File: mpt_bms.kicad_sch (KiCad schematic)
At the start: 25 parts, among them U4 TPS62590, U5 BQ25185, U6 BQ27441-G1

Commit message: Added Display
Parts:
- C2: renamed from C109; footprint passive:C_0603 -> passive:C_0805; symbol db:capacitor/01.018.0025.0003 -> db:capacitor/01.018.0008.0004; Dist1# 311-1785-1-ND -> 311-1885-1-ND; FP C_0603 -> C_0805; MFR# CC0603KRX5R7BB475 -> CC0805KKX7R8BB475; Modified 2026-03-22 17:14:39 -> 2026-10-07 15:04:34; Rating 16V 10% -> 25V 10%; Series CC-X7R -> CC-X5R
- C8: renamed from C3; symbol db:capacitor/01.018.0025.0002 -> db:capacitor/01.018.0025.0013; Dist1# 311-1446-1-ND -> 311-2082-1-ND; MFR# CC0603KRX7R7BB105 -> CC0603KRX7R9BB105; Modified 2026-03-22 17:11:33 -> 2026-10-07 18:52:36; Rating 16V 10% -> 50V 10%
- D1: value Orange -> Red; footprint diode:D_0603 -> diode:LED_0805_Right_Angle; symbol db:diode/05.035.0031.0003 -> db:diode/05.035.0031.0004; Dist1# 160-1434-1-ND -> 160-1469-1-ND; Dist2 mouser -> none; FP D_0603 -> LED_0805_Right_Angle; MFR# LTST-C190KFKT -> LTST-S220KRKT; Modified 2026-03-23 15:41:47 -> 2026-10-06 21:05:36; Rating 2v 20mA 605nm -> 20mA; Version 2 -> 1
- R10: renamed from R15; symbol db:resistor/00.018.0009.0034 -> db:resistor_0603/00.018.0009.0578; Dist1# 13-RT0603FRE07619KLCT-ND -> 311-619KHRCT-ND; MFR# RT0603FRE07619KL -> RC0603FR-07619KL; Modified 2026-09-18 19:20:11 -> 2026-10-07 14:47:41; Rating 100mW, 1% -> 125mW, 1%; Remarks (none) -> Autogenerated; Version 1 -> 2
- R11: renamed from R16; symbol db:resistor/00.018.0009.0025 -> db:resistor_0603/00.018.0009.0139; Modified 2026-07-27 12:47:10 -> 2026-10-07 14:47:41; Rating 100mW, 1% -> 125mW, 1%; Remarks (none) -> Autogenerated
- R12: renamed from R17; symbol db:resistor/00.018.0009.0006 -> db:resistor_0603/00.018.0009.0046; Modified 2026-02-11 09:36:06 -> 2026-10-07 14:47:41; Rating 100mW, 1% -> 125mW, 1%; Remarks (none) -> Autogenerated
- R13: renamed from R18; symbol db:resistor/00.018.0009.0006 -> db:resistor_0603/00.018.0009.0046; Modified 2026-02-11 09:36:06 -> 2026-10-07 14:47:41; Rating 100mW, 1% -> 125mW, 1%; Remarks (none) -> Autogenerated
- R14: renamed from R19; symbol db:resistor/00.018.0009.0006 -> db:resistor_0603/00.018.0009.0046; Modified 2026-02-11 09:36:06 -> 2026-10-07 14:47:41; Rating 100mW, 1% -> 125mW, 1%; Remarks (none) -> Autogenerated
- R15: renamed from R20; symbol db:resistor/00.018.0011.0002 -> db:resistor_0603/00.018.0011.0002
- R6: renamed from R11; symbol db:resistor/00.018.0009.0006 -> db:resistor_0603/00.018.0009.0046; Modified 2026-02-11 09:36:06 -> 2026-10-07 14:47:41; Rating 100mW, 1% -> 125mW, 1%; Remarks (none) -> Autogenerated
- R7: renamed from R12; symbol db:resistor/00.018.0009.0033 -> db:resistor_0603/00.018.0009.0124; Dist1# 13-RT0603FRE0713KLCT-ND -> 311-13.0KHRCT-ND; MFR# RT0603FRE0713KL -> RC0603FR-0713KL; Modified 2026-09-17 21:00:44 -> 2026-10-07 14:47:41; Rating 100mW, 1% -> 125mW, 1%; Remarks (none) -> Autogenerated; Version 1 -> 2
- R8: renamed from R13; symbol db:resistor/00.018.0009.0006 -> db:resistor_0603/00.018.0009.0046; Modified 2026-02-11 09:36:06 -> 2026-10-07 14:47:41; Rating 100mW, 1% -> 125mW, 1%; Remarks (none) -> Autogenerated
- R9: renamed from R14; symbol db:resistor/00.018.0009.0036 -> db:resistor_0603/00.018.0009.0638; Modified 2026-10-05 20:40:11 -> 2026-10-07 14:47:41; Rating 100mW, 1% -> 125mW, 1%; Remarks (none) -> Autogenerated
- U2: renamed from U5; symbol db:ic/07.015.0001.0001 -> db:power_ic/07.015.0001.0001; Category ic -> power_ic
- U3: renamed from U6; symbol db:ic/07.015.0001.0002 -> db:power_ic/07.015.0001.0002; Category ic -> power_ic
- renumbered BT3 to BT1, BT4 to BT2, C5 to C1, C6 to C3, C7 to C5, C9 to C6, C8 to C7, L2 to L1, U4 to U1
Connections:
- net GND: now also U1.7 (PAD), U2.0 (PAD), U3.0 (PAD)
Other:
- note added: "1100mA input current limit +4V2 Charge Cutoff Voltage"
- note added: "390mA charge current limit R_{iset} = 300/I_{chrg}"
- note added: "Each holder holds a 3.7V 10440 LI-ION Cell with protection Type used: Keeppower 10440 - 570mAh 3.6V P1044C"
- note removed: "1100mA in current limit +4V2 Battery Voltage"
- note removed: "390mA charge current limit"
- note removed: "Each holder holds a 3.7V 10440 LI-ION Cell with protection"
- note removed: "change to sidewards facing diode"
- moved on the sheet: C7, C8, D1, R13, R14, R15, U3

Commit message: Added Sheets for optional Buzzer and User Buttons
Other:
- note added: "VDD Anschliessen"
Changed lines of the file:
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@@
+		)
+	)
+	(text "VDD Anschliessen"
+		(exclude_from_sim no)
+		(at 228.854 75.184 0)
+		(effects
+			(font
+				(size 1.27 1.27)
+			)
 		)
 	)

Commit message: Work in Progress of RTC Added Sheet Titles
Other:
- company: (none) -> Hochschule Luzern, Technik & Architektur
- title: M.P.T.H BMS -> M.P.T BMS
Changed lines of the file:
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@@
 	(paper "A4")
 	(title_block
-		(title "M.P.T.H BMS")
+		(title "M.P.T BMS")
+		(company "Hochschule Luzern, Technik & Architektur")
 	)
 	(rectangle

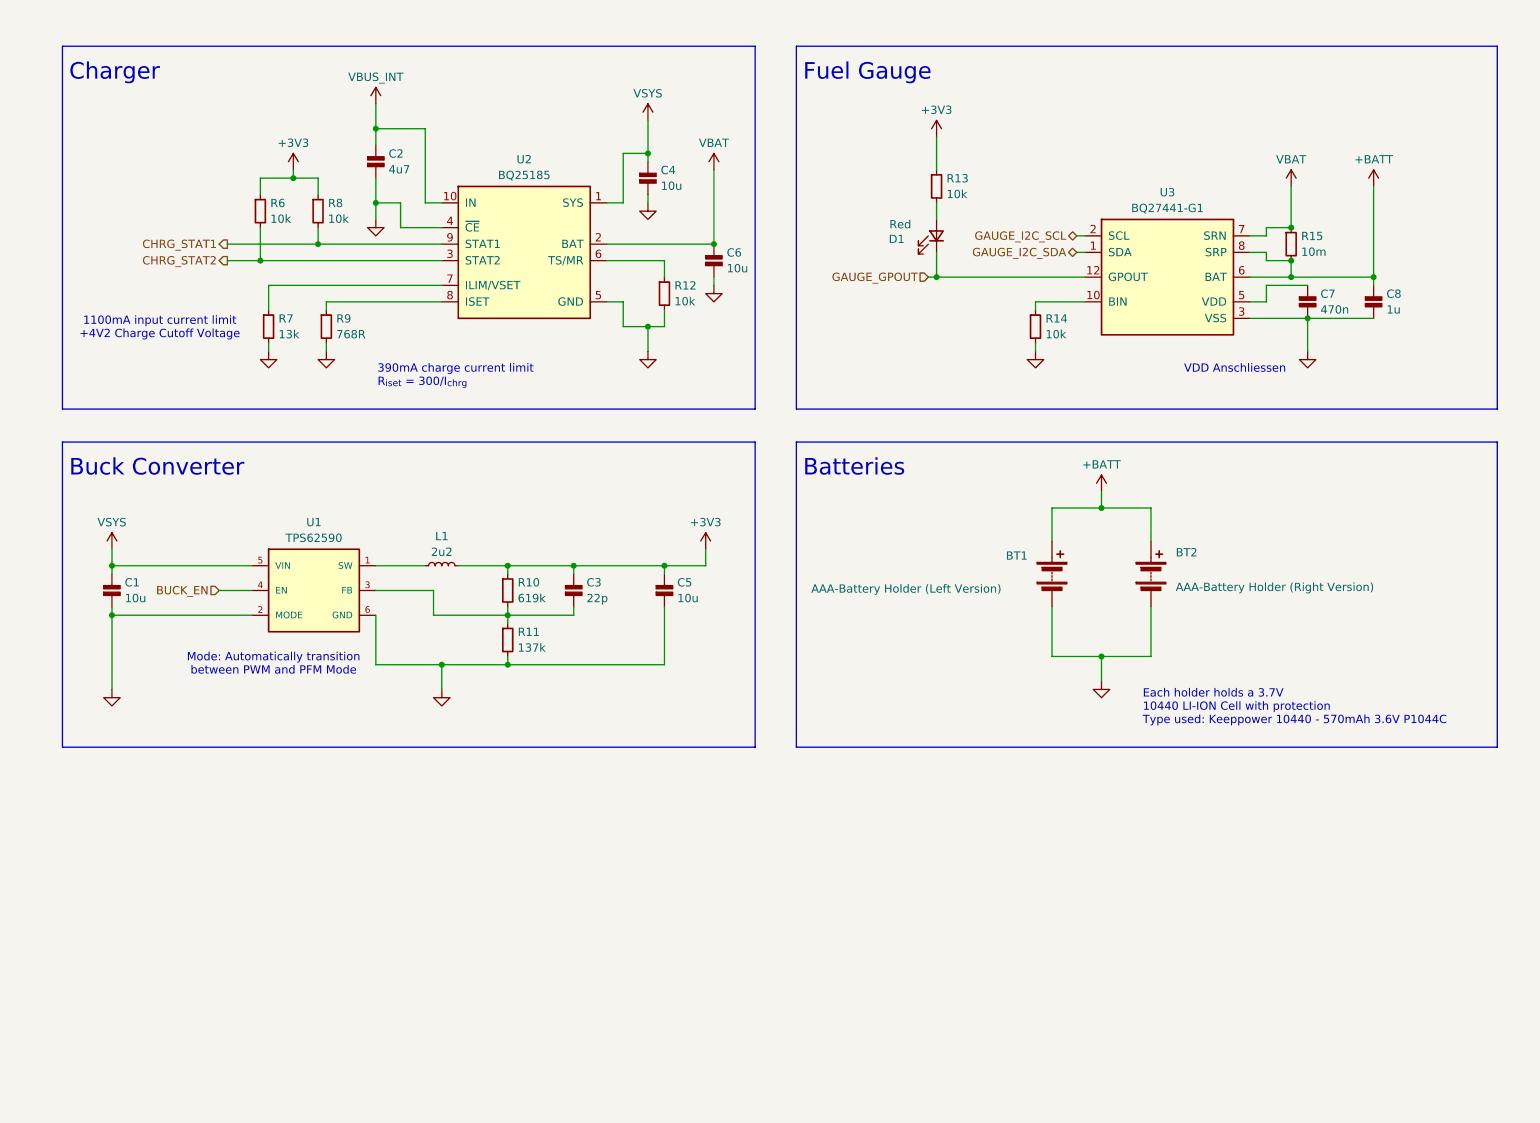
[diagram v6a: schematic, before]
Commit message: Change Buck Converter to Buck-Boost Add charge indicator LEDs Remove indicator LED from fuel gauge
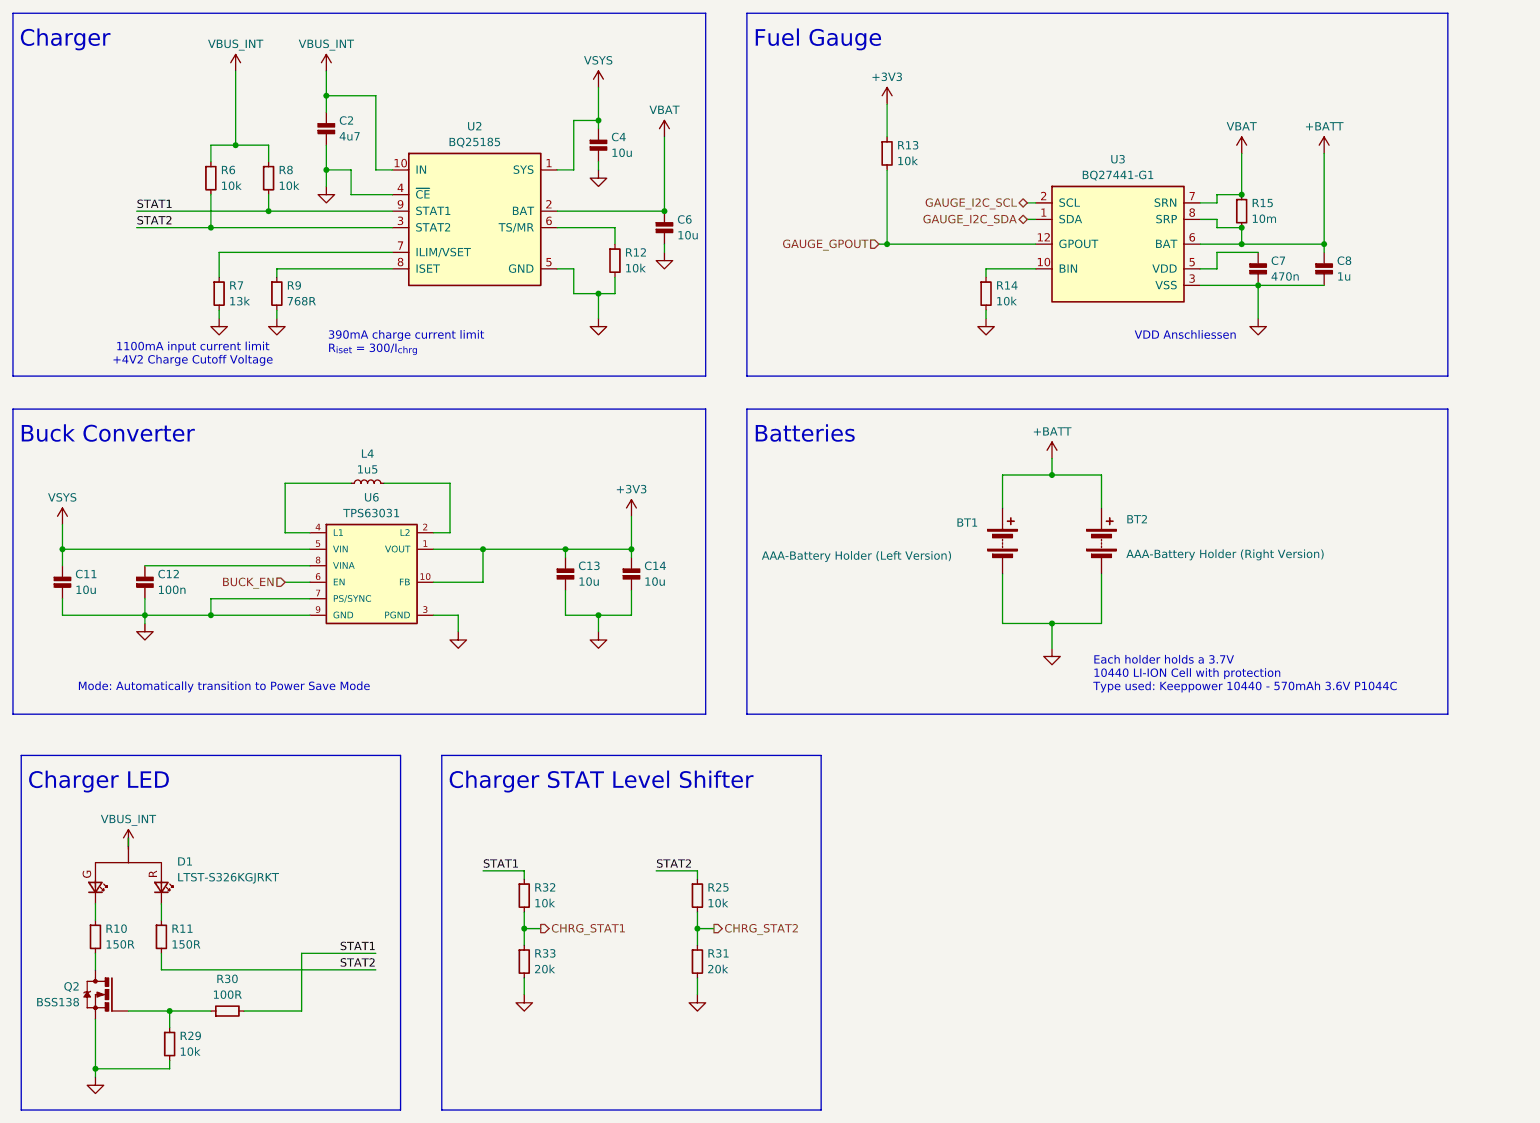
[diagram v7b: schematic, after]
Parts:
- removed C1, C5: 10u, passive:C_0603, symbol db:capacitor/01.018.0008.0001
- removed C3: 22p, passive:C_0603, symbol db:capacitor/01.018.0025.0012
- removed D1: Red, diode:LED_0805_Right_Angle, symbol db:diode/05.035.0031.0004
- removed L1: 2u2, passive:L_3.2mmx2.5mm, symbol db:inductor/02.002.0006.0001
- removed R10: 619k, passive:R_0603, symbol db:resistor_0603/00.018.0009.0578
- removed R11: 137k, passive:R_0603, symbol db:resistor_0603/00.018.0009.0139
- removed U1: TPS62590, package:WSON-6-1EP_2x2mm_P0.65mm, symbol db:power_ic/11.015.0044.0001
- added C11, C13, C14: 10u, passive:C_0603, symbol db:capacitor/01.018.0008.0001
- added C12: 100n, passive:C_0603, symbol db:capacitor/01.018.0025.0014
- added D1: LTST-S326KGJRKT, diode:LED_RG_0805_Right_Angle, symbol db:led/08.035.0031.0001
- added L4: 1u5, passive:L_Coilcraft_LPS301X, symbol db:inductor/02.045.0052.0001
- added Q2: BSS138, package:SOT-23, symbol db:mosfet/03.011.0000.0001
- added R10, R11: 150R, passive:R_0603, symbol db:resistor_0603/00.018.0009.0164
- added R25, R29, R32: 10k, passive:R_0603, symbol db:resistor_0603/00.018.0009.0046
- added R30: 100R, passive:R_0603, symbol db:resistor_0603/00.018.0009.0044
- added R31, R33: 20k, passive:R_0603, symbol db:resistor_0603/00.018.0009.0250
- added U6: TPS63031, package:WSON-10-1EP_2.5x2.5mm_P0.5mm, symbol db:power_ic/11.015.0044.0002
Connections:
- net +3V3: now also C13.1, C14.1, U6.1 (VOUT), U6.10 (FB); no longer R6.1, R8.1
- net BUCK_EN: now also U6.6 (EN)
- net CHRG_STAT1: now also R32.2, R33.1; no longer R8.2, U2.9 (STAT1)
- net CHRG_STAT2: now also R25.2, R31.1; no longer R6.2, U2.3 (STAT2)
- net GAUGE_GPOUT: now also R13.2
- net GND: now also C11.2, C12.2, C13.2, C14.2, Q2.2 (S), R29.2, R31.2, R33.2, U6.0 (PAD), U6.3 (PGND), U6.7 (PS/SYNC), U6.9 (GND)
- net VBUS_INT: now also R6.1, R8.1, D1.2 (A)
- net VSYS: now also C11.1, U6.5 (VIN)
- new net: D1.4 (C_G), R10.1
- new net: Q2.3 (D), R10.2
- new net: C12.1, U6.8 (VINA)
- new net: L4.2, U6.2 (L2)
- new net: L4.1, U6.4 (L1)
- new net: D1.1 (C_R), R11.1
- new net: Q2.1 (G), R29.1, R30.1
- new net STAT1: R30.2, R32.1, R8.2, U2.9 (STAT1)
- new net STAT2: R11.2, R25.1, R6.2, U2.3 (STAT2)
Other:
- note added: "Charger LED"
- note added: "Charger STAT Level Shifter"
- note added: "Mode: Automatically transition to Power Save Mode"
- note removed: "Mode: Automatically transition between PWM and PFM Mode"
- moved on the sheet: BT1, BT2, C2, C4, C6, C7, C8, R12, R13, R14, R15, R6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
